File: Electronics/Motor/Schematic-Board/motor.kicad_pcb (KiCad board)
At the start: 2 copper layers, 45 x 45 mm, 74 parts, among them J1 CONN_02X05, J11 V, J12 U, J13 W, J2 RS485, J3 RS485, J4 CONN_01X06, J5 JTAG, J6 12, J9 GND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

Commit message: current work
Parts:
- removed the REF** at (81.5, 65.5)
- removed the REF** at (78.5, 63.6)
- added J7: CONN_01X06, Dizzy:SPI_CONN, F.Cu at (75.0, 68.2)
- J4: footprint SPI_BIG -> Dizzy:SPI_CONN

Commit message: saving changes
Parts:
- D5: footprint LEDs:LED_0603 -> LEDs:LED_0805_HandSoldering
- moved J4 6.15 mm to (76.6, 68.2)
- moved J7 2.30 mm to (72.8, 68.2)
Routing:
- net MISO: track 40.2 -> 33.6 mm
- net SCK: track 40.3 -> 34.2 mm
- net MOSI: track 42.6 -> 36.5 mm
- net +3V3: track 99.0 -> 96.8 mm
- net CS_EXTERNAL: track 40.7 -> 38.8 mm

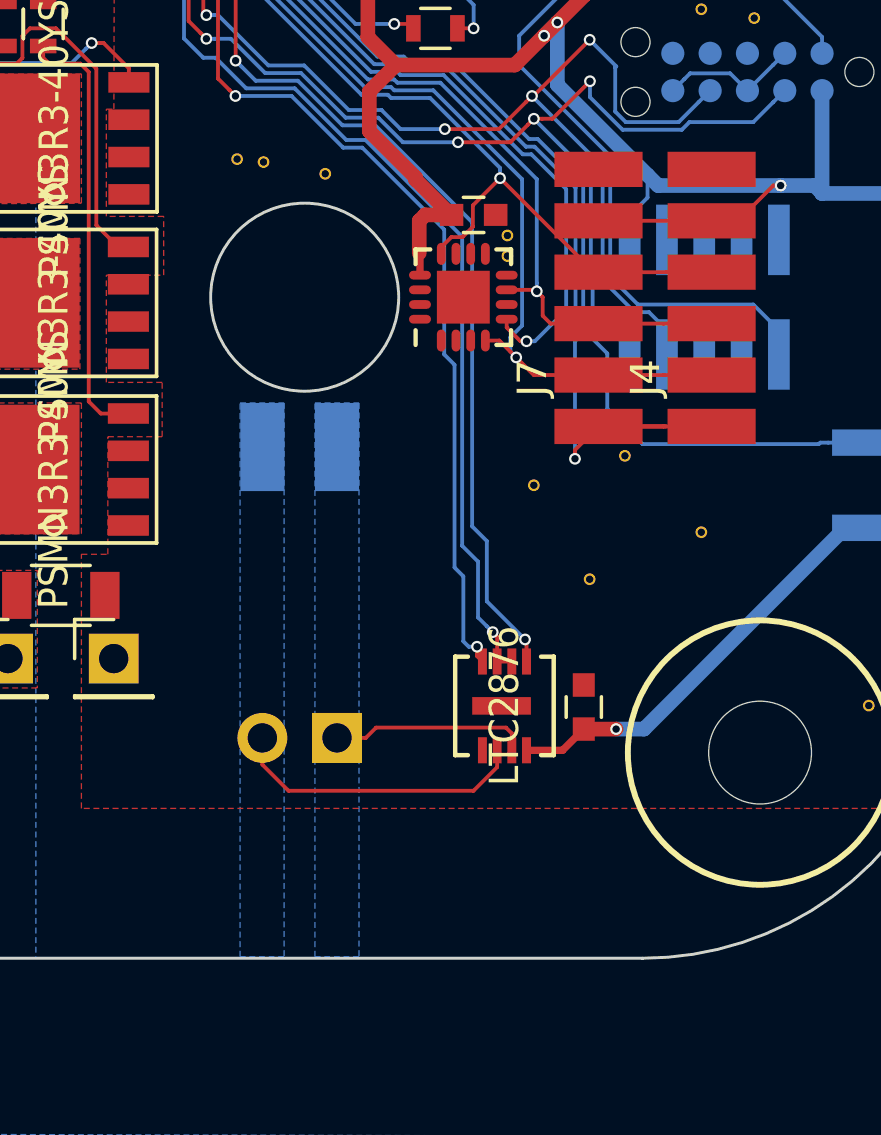
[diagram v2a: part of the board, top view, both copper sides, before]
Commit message: gyro is working
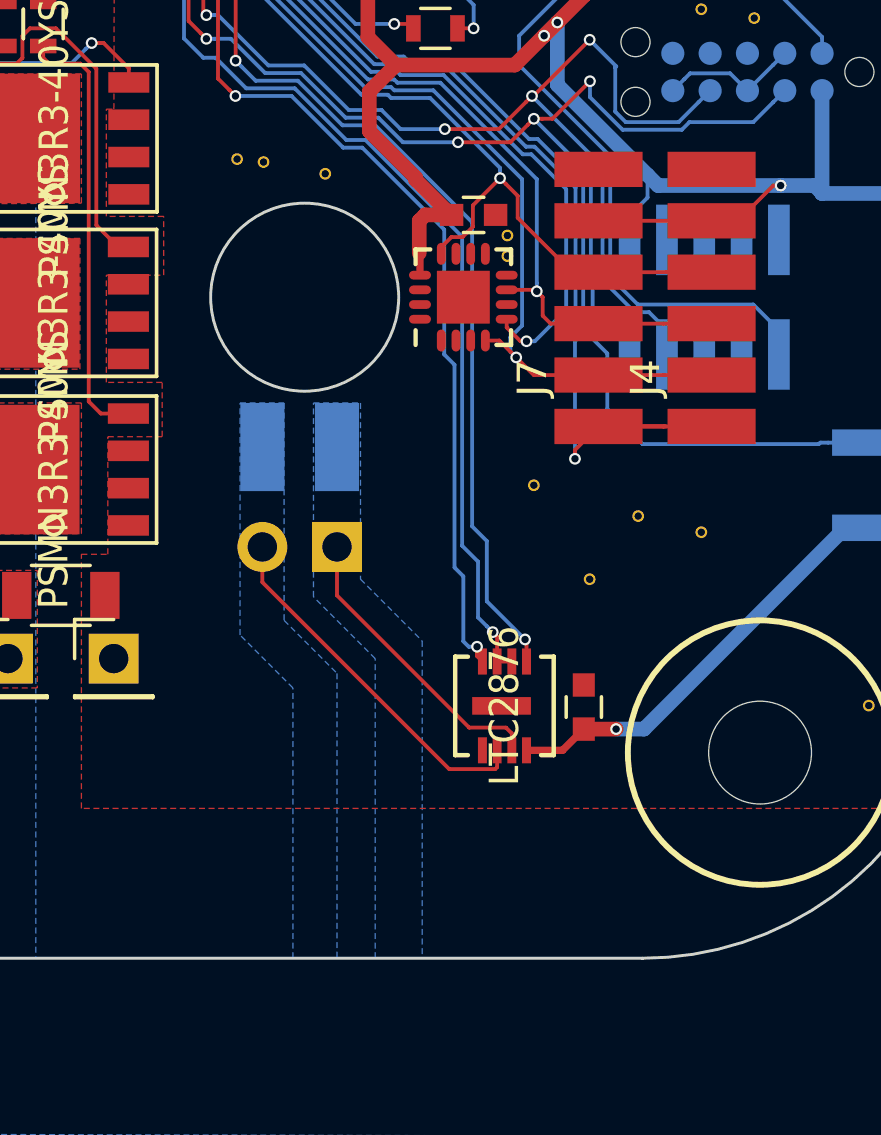
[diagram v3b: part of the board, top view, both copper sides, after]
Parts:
- moved J3 6.50 mm to (66.6, 74.0)
- moved REF** 2.10 mm to (77.0, 73.0)
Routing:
- net RS-B: track 6.75 -> 10.1 mm
- net RS-A: track 10.2 -> 12.4 mm
- net SCK: track 34.2 -> 34.8 mm
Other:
- board text removed: "RS485 B A"
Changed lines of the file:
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@@
     (links 150)
     (no_connects 0)
-    (area 42.949999 42.949999 88.050001 88.050001)
+    (area 36.25 38.65 94.000001 94.100001)
     (thickness 1.6)
-    (drawings 18)
-    (tracks 622)
+    (drawings 17)
+    (tracks 626)
     (zones 0)
     (modules 73)
@@
   )
   (module Pin_Headers:Pin_Header_Straight_1x02_Pitch2.54mm (layer B.Cu)
-    (at 66.6 80.5 90)
+    (at 66.6 74 90)
     (descr "Through hole straight pin header, 1x02, 2.54mm pitch, single row")
     (tags "Through hole pin header THT 1x02 2.54mm single row")
@@
   )
   (module Dizzy:VIA-0.4 (layer F.Cu)
-    (at 76.5 70.9)
+    (at 76.95 72.95)
     (fp_text reference REF** (at 0 0.5) (layer F.SilkS) hide
       (effects (font (size 0.127 0.127) (thickness 0.03175)))
@@
   (gr_text ID (at 81 72) (layer B.Mask)
     (effects (font (size 1.2 1.2) (thickness 0.3)) (justify mirror))
-  )
-  (gr_text "RS485\nB A" (at 72.1 83.1) (layer B.Mask)
-    (effects (font (size 1.2 1.2) (thickness 0.25)) (justify mirror))
   )
   (gr_text DizzyRobot (at 73.3 46.4) (layer B.Mask)
@@
   (segment (start 65.05 46.6) (end 65.05 46.95) (width 0.13) (layer F.Cu) (net 18))
   (via (at 62.665825 49.217677) (size 0.4) (drill 0.25) (layers F.Cu B.Cu) (net 18))
+  (segment (start 75.5 64.65) (end 74.6 64.65) (width 0.13) (layer F.Cu) (net 19))
+  (segment (start 74.6 64.65) (end 72.75 62.8) (width 0.13) (layer F.Cu) (net 19))
+  (segment (start 72.75 62.8) (end 72.75 62.05) (width 0.13) (layer F.Cu) (net 19))
+  (segment (start 72.75 62.05) (end 72.349999 61.649999) (width 0.13) (layer F.Cu) (net 19))
+  (segment (start 72.349999 61.649999) (end 72.15 61.45) (width 0.13) (layer F.Cu) (net 19))
   (segment (start 77.8 64.65) (end 79.35 64.65) (width 0.13) (layer F.Cu) (net 19))
   (segment (start 77.8 64.65) (end 75.35 64.65) (width 0.13) (layer F.Cu) (net 19))
-  (segment (start 72.15 61.45) (end 75.35 64.65) (width 0.13) (layer F.Cu) (net 19))
   (segment (start 72.15 61.45) (end 71.225 62.375) (width 0.13) (layer F.Cu) (net 19))
   (segment (start 71.225 62.375) (end 71.225 63.101002) (width 0.13) (layer F.Cu) (net 19))
@@
   (via (at 62.05 50.85) (size 0.4) (drill 0.25) (layers F.Cu B.Cu) (net 19))
   (via (at 72.15 61.45) (size 0.4) (drill 0.25) (layers F.Cu B.Cu) (net 19))
-  (segment (start 66.6 80.5) (end 67.58 80.5) (width 0.13) (layer F.Cu) (net 20))
-  (segment (start 67.58 80.5) (end 67.93 80.15) (width 0.13) (layer F.Cu) (net 20))
-  (segment (start 67.93 80.15) (end 72.3519 80.15) (width 0.13) (layer F.Cu) (net 20))
-  (segment (start 72.3519 80.15) (end 72.55 80.3481) (width 0.13) (layer F.Cu) (net 20))
-  (segment (start 72.55 80.3481) (end 72.55 80.9226) (width 0.13) (layer F.Cu) (net 20))
-  (segment (start 64.06 80.5) (end 64.06 81.41) (width 0.13) (layer F.Cu) (net 21))
-  (segment (start 64.06 81.41) (end 64.95 82.3) (width 0.13) (layer F.Cu) (net 21))
-  (segment (start 64.95 82.3) (end 71.2471 82.3) (width 0.13) (layer F.Cu) (net 21))
-  (segment (start 71.2471 82.3) (end 72.05 81.4971) (width 0.13) (layer F.Cu) (net 21))
-  (segment (start 72.05 81.4971) (end 72.05 80.9226) (width 0.13) (layer F.Cu) (net 21))
+  (segment (start 72.55 80.9226) (end 72.55 80.3481) (width 0.13) (layer F.Cu) (net 20))
+  (segment (start 72.55 80.3481) (end 72.3519 80.15) (width 0.13) (layer F.Cu) (net 20))
+  (segment (start 72.3519 80.15) (end 71.1 80.15) (width 0.13) (layer F.Cu) (net 20))
+  (segment (start 71.1 80.15) (end 66.6 75.65) (width 0.13) (layer F.Cu) (net 20))
+  (segment (start 66.6 75.65) (end 66.6 74) (width 0.13) (layer F.Cu) (net 20))
+  (segment (start 72.05 80.9226) (end 72.05 81.4971) (width 0.13) (layer F.Cu) (net 21))
+  (segment (start 72.05 81.4971) (end 71.984999 81.562101) (width 0.13) (layer F.Cu) (net 21))
+  (segment (start 71.984999 81.562101) (end 70.42002 81.562101) (width 0.13) (layer F.Cu) (net 21))
+  (segment (start 70.42002 81.562101) (end 64.06 75.202081) (width 0.13) (layer F.Cu) (net 21))
+  (segment (start 64.06 75.202081) (end 64.06 74) (width 0.13) (layer F.Cu) (net 21))
   (segment (start 50.1 68.95) (end 50.1 69.43) (width 0.13) (layer F.Cu) (net 22))
   (segment (start 55.05 56.95) (end 54.25 56.15) (width 0.13) (layer F.Cu) (net 22))
@@
     (polygon
       (pts
-        (xy 63.3 69.1) (xy 64.8 69.1) (xy 64.8 87.95) (xy 63.3 87.95)
+        (xy 63.3 69.1) (xy 64.8 69.1) (xy 64.8 76.5) (xy 66.6 78.3) (xy 66.6 88)
+        (xy 65.1 88) (xy 65.1 78.8) (xy 63.3 77)
       )
     )
@@
     (polygon
       (pts
-        (xy 65.85 69.1) (xy 67.35 69.1) (xy 67.35 87.95) (xy 65.85 87.95)
+        (xy 65.8 69.1) (xy 67.4 69.1) (xy 67.4 75.1) (xy 69.5 77.2) (xy 69.5 88)
+        (xy 67.9 88) (xy 67.9 77.8) (xy 65.8 75.7)
       )
     )
@@
     (polygon
       (pts
-        (xy 65.85 69.1) (xy 67.35 69.1) (xy 67.35 87.95) (xy 65.85 87.95)
+        (xy 65.8 69.1) (xy 67.4 69.1) (xy 67.4 75.1) (xy 69.5 77.2) (xy 69.5 88)
+        (xy 67.9 88) (xy 67.9 77.8) (xy 65.8 75.7)
       )
     )
@@
     (polygon
       (pts
-        (xy 63.3 69.1) (xy 64.8 69.1) (xy 64.8 87.95) (xy 63.3 87.95)
+        (xy 63.3 69.1) (xy 64.8 69.1) (xy 64.8 76.5) (xy 66.6 78.3) (xy 66.6 88)
+        (xy 65.1 88) (xy 65.1 78.8) (xy 63.3 77)
       )
     )
